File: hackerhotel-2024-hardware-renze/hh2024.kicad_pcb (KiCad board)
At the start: 2 copper layers, 95 parts, among them J1 SAO_connector, SW1 Multi-Directional-Switches, SW2 Multi-Directional-Switches, SW3 Multi-Directional-Switches, SW4 Multi-Directional-Switches, SW5 Multi-Directional-Switches

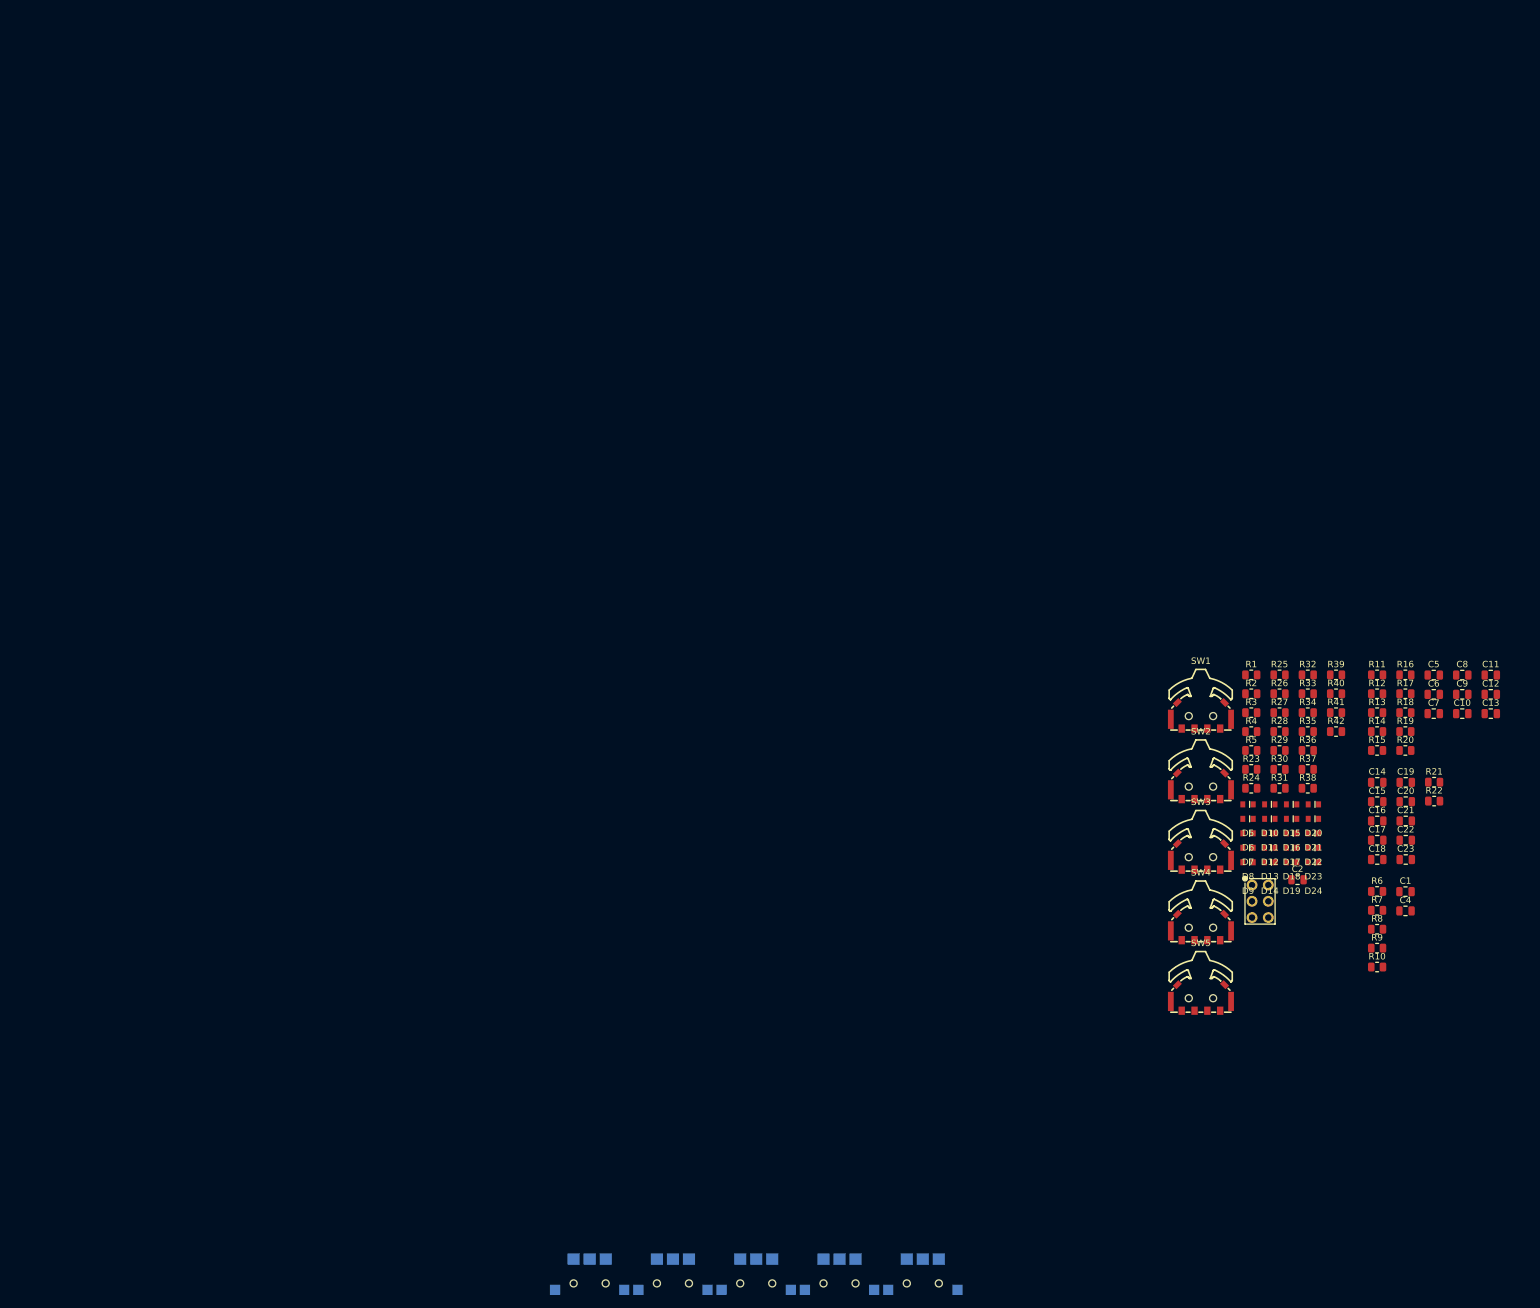
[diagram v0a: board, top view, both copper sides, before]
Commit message: Started layout
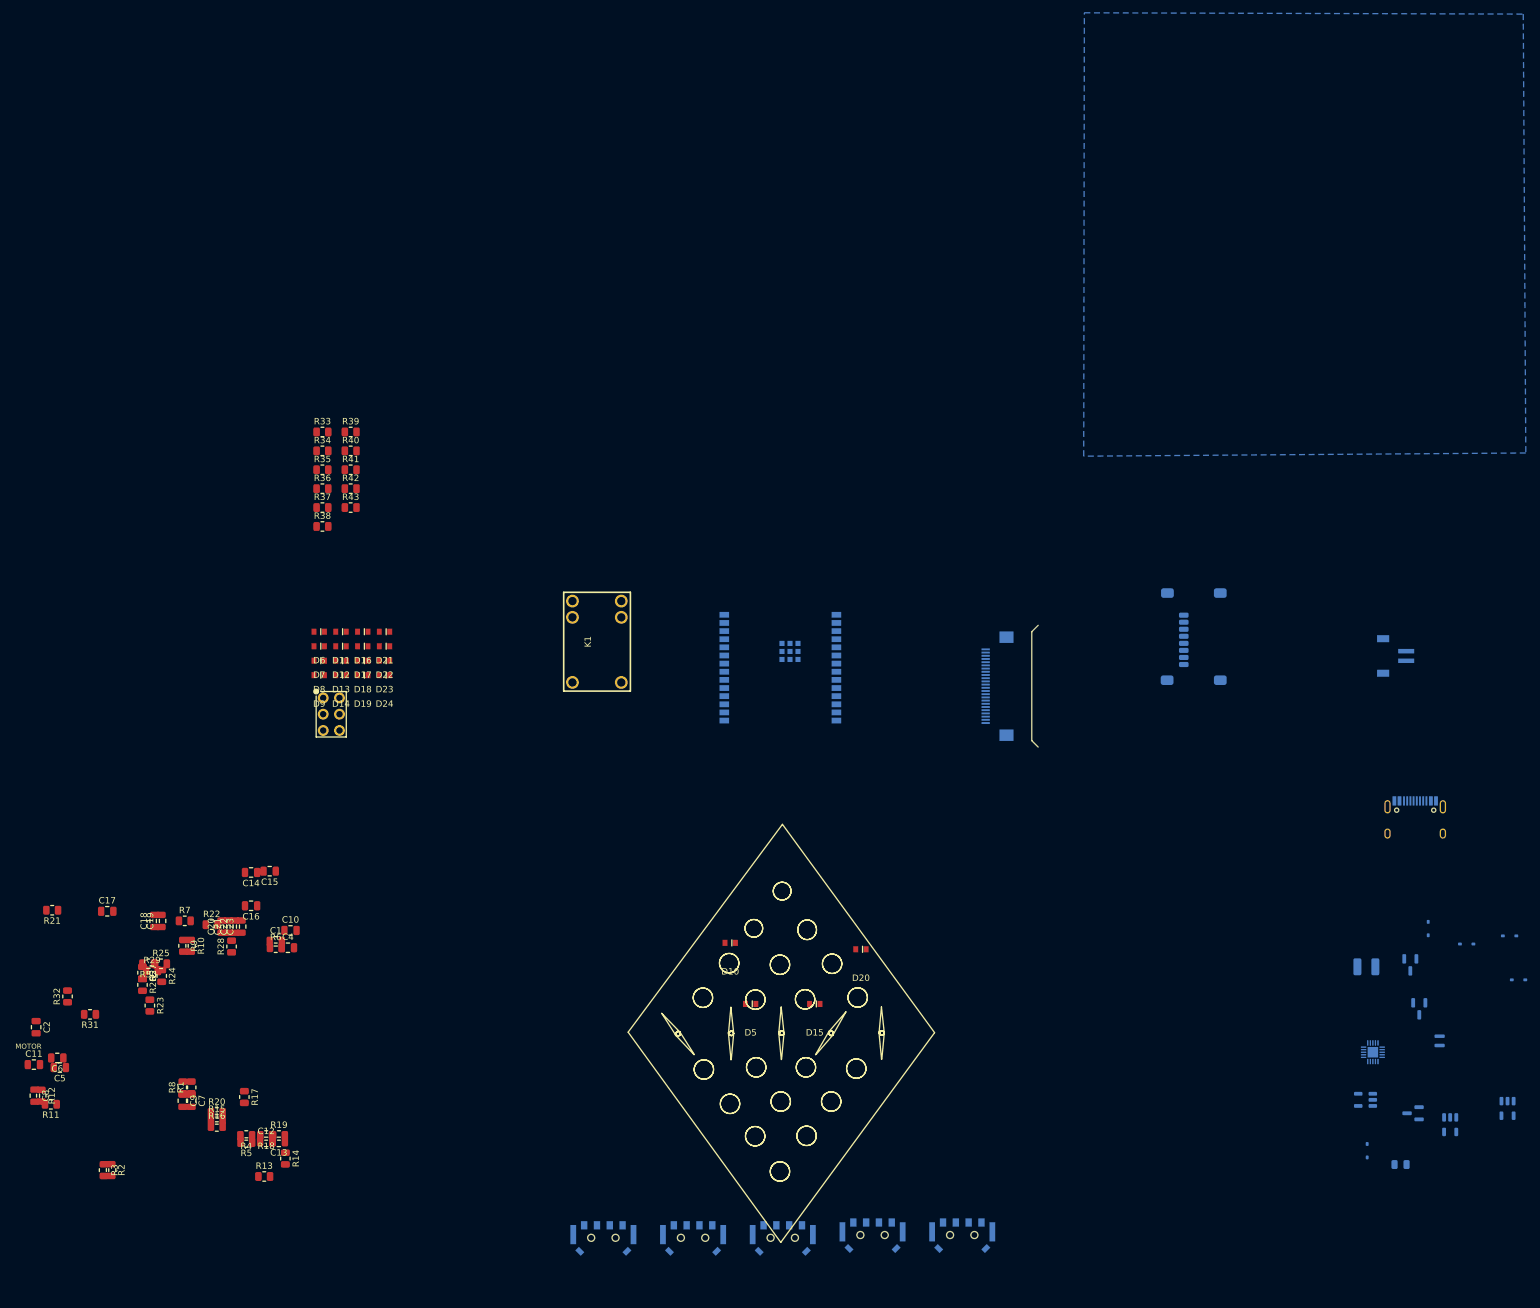
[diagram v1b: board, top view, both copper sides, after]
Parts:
- removed REF** (x5): TM-2022-2, BamboulabFootprints:TM-2022-2
- added D1: NSVR0320MW2T1G, tanoshii:D_SOD-323, B.Cu at (223.3, 138.5)
- added D2: NSVR0320MW2T1G, tanoshii:D_SOD-323, B.Cu at (245.6, 105.0)
- added D25: NSVR0320MW2T1G, tanoshii:D_SOD-323, B.Cu at (247.0, 111.8)
- added D3: NSVR0320MW2T1G, tanoshii:D_SOD-323, B.Cu at (238.9, 106.2)
- added D4: NSVR0320MW2T1G, tanoshii:D_SOD-323, B.Cu at (232.9, 103.8)
- added F1: 1A, tanoshii:Fuse_0805_2012Metric, B.Cu at (228.6, 140.7)
- added J3: Micro_SD_Card, tanoshii:MicroSD-SOFNG-TF-002-H18, B.Cu at (194.8, 58.2)
- added J4: USB-C, tanoshii:USB_C_Receptacle_HRO_TYPE-C-31-M-12, B.Cu at (230.8, 88.0)
- added J5: Battery, tanoshii:JST_S2B-ZR-SM4A-TF(LF)(SN), B.Cu at (227.3, 61.3)
- added J6: E-Paper, tanoshii:Hirose_FH12-24S-0.5SH_1x24-1MP_P0.50mm_Horizontal, B.Cu at (165.7, 66.0)
- added K1: SANYOU_SRD_Form_C, BamboulabFootprints:HRS1H-S-DC3V, F.Cu at (103.1, 59.1)
- added L1: 2.2u, tanoshii:Inductor_MSC20FC, B.Cu at (234.7, 121.4)
- added L2: 47u, tanoshii:L_1210_3225Metric, B.Cu at (223.2, 109.8)
- added Q1: AP2302B, tanoshii:SOT-23, B.Cu at (230.5, 132.7)
- added Q2: AP2302B, tanoshii:SOT-23, B.Cu at (230.1, 109.5)
- added Q3: AP2302B, tanoshii:SOT-23, B.Cu at (231.5, 116.4)
- added R43: 10k, Resistor_SMD:R_0805_2012Metric, F.Cu at (64.7, 38.1)
- added U1: ESP32-C6-WROOM-1, tanoshii:ESP32-C6-WROOM-1, B.Cu at (131.8, 63.1)
- added U2: SY8079AAC, tanoshii:SOT-23-5, B.Cu at (245.3, 131.9)
- added U3: XT4054K421MR-G, tanoshii:SOT-23-5, B.Cu at (236.3, 134.4)
- added U4: SY6280AAC, tanoshii:SOT-23-5, B.Cu at (223.1, 130.6)
- added U5: CH32V003F4U6, vfd:QFN-20-1EP_3x3mm_P0.4mm_EP1.65x1.65mm, B.Cu at (224.2, 123.1)
- J1: value SAO_connector -> SAO
- SW1, SW2, SW3, SW4, SW5: moved to B.Cu
- moved C11 235.4 mm to (15.3, 125.1)
- moved C8 232.3 mm to (15.4, 129.9), turned to -90 degrees
- moved C5 223.0 mm to (19.3, 125.5), turned to 180 degrees
- moved C6 222.2 mm to (18.9, 124.0), turned to 180 degrees
- moved R12 217.7 mm to (16.4, 129.9), turned to -90 degrees
- moved R11 217.6 mm to (17.9, 131.3), turned to 180 degrees
- moved R21 216.6 mm to (18.1, 101.0), turned to 180 degrees
- moved C9 209.5 mm to (38.5, 130.7), turned to -90 degrees
- moved C12 203.5 mm to (51.5, 137.1)
- moved C7 203.1 mm to (39.8, 130.7), turned to -90 degrees
- moved C13 200.6 mm to (53.5, 137.1), turned to 180 degrees
- moved R32 200.0 mm to (20.5, 114.4), turned to 90 degrees
- moved C17 198.5 mm to (26.7, 101.1)
- moved R16 198.4 mm to (43.8, 134.7)
- moved C2 198.2 mm to (15.6, 119.2), turned to -90 degrees
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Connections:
- J1 pad 5: unconnected-(J1-IO1-Pad5) -> /microcontroller/SAO IO1
- J1 pad 6: unconnected-(J1-IO2-Pad6) -> /microcontroller/SAO IO2
- R28 pad 2: MSW1L -> MSWL
- R29 pad 2: MSW1B -> MSWB
- R30 pad 2: MSW1R -> MSWR
- R31 pad 2: MSW2R -> MSWR
- R32 pad 2: MSW2B -> MSWB
- R33 pad 2: MSW2L -> MSWL
- R34 pad 2: MSW3R -> MSWR
- R35 pad 2: MSW3B -> MSWB
- R36 pad 2: MSW3L -> MSWL
- R37 pad 2: MSW4R -> MSWR
- R38 pad 2: MSW4B -> MSWB
- R39 pad 2: MSW4L -> MSWL
- R40 pad 2: MSW5R -> MSWR
- R41 pad 2: MSW5B -> MSWB
- R42 pad 2: MSW5L -> MSWL
- R8 pad 2: MSW2L -> /microcontroller/Relay Ctrl
- SW1 pad 1: GND -> MSWR
- SW1 pad 2: MSW1R -> MSWL
- SW1 pad C: (no net) -> MSWS1
- SW1 pad T: (no net) -> MSWB
- SW2 pad 1: GND -> MSWR
- SW2 pad 2: MSW2R -> MSWL
- SW2 pad C: (no net) -> MSWS2
- SW2 pad T: (no net) -> MSWB
- SW3 pad 1: GND -> MSWR
- SW3 pad 2: MSW3R -> MSWL
- SW3 pad C: (no net) -> MSWS3
- SW3 pad T: (no net) -> MSWB
- SW4 pad 1: unconnected-(SW4-C-Pad1) -> MSWR
- SW4 pad 2: MSW4R -> MSWL
- SW4 pad C: (no net) -> MSWS4
- SW4 pad T: (no net) -> MSWB
- SW5 pad 1: GND -> MSWR
- SW5 pad 2: MSW5R -> MSWL
- SW5 pad C: (no net) -> MSWS5
- SW5 pad T: (no net) -> MSWB
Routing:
- added copper zone on B.Cu, net GND
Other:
- board outline added: 1 x 19 mm
- board text added: "MOTOR"

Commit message: removed extra pull ups on multi switches
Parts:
- C1, C4, R10, R6, R7, R8, R9: moved to B.Cu
- R23, R24, R25, R26, R27: value R_Small -> 30
- moved R18 506.5 mm to (558.0, 139.7)
- moved R1 496.1 mm to (429.3, 436.0)
- moved C10 491.9 mm to (510.4, 290.8)
- moved C11 491.9 mm to (470.3, 311.8)
- moved C5 491.9 mm to (474.4, 312.2)
- moved C6 491.9 mm to (474.0, 310.7)
- moved C8 491.9 mm to (470.5, 316.6)
- moved R11 491.9 mm to (473.0, 318.0)
- moved R12 491.9 mm to (471.5, 316.6)
- moved C13 465.9 mm to (519.1, 152.4)
- moved R19 465.9 mm to (519.1, 151.4)
- moved J3 456.9 mm to (416.0, 458.0)
- moved R15 456.4 mm to (489.9, 230.1)
- moved R16 456.4 mm to (489.9, 231.2)
- moved R17 456.4 mm to (494.2, 226.6)
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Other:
- board size 1 x 19 mm -> 80 x 113 mm

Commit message: Routing complete (apart from LEDs)
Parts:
- removed R31, R32, R33, R34, R35, R36, R37, R38, R39, R40, R41, R42: 10k, Resistor_SMD:R_0805_2012Metric
- added J2: Breakout pads, Connector_PinHeader_2.54mm:PinHeader_1x03_P2.54mm_Vertical, B.Cu at (108.7, 64.8)
- C10, C11, C12, C13, C14, C15, C16, C17, C18, C19, C2, C20, C21, C22, C23, C5, C6, C7, C8, C9, D10, D11, D12, D13, D14, D15, D16, D17, D18, D19, D20, D21, D22, D23, D24, D5, D6, D7, D8, D9, J1, R1, R11, R12, R13, R14, R15, R16, R17, R18, R19, R2, R20, R21, R22, R23, R24, R25, R26, R27, R28, R29, R3, R30, R4, R43, R5: moved to B.Cu
- moved J3 513.4 mm to (96.8, 55.8)
- moved R1 498.8 mm to (107.7, 54.6)
- moved R18 457.4 mm to (102.7, 95.5), turned to 0 degrees
- moved C13 426.4 mm to (97.1, 91.4)
- moved R19 426.0 mm to (97.1, 93.5)
- moved U2 425.2 mm to (149.8, 90.3)
- moved D1 418.9 mm to (121.4, 84.2), turned to 90 degrees
- moved Q1 414.4 mm to (130.8, 85.2), turned to 0 degrees
- moved C10 414.4 mm to (149.8, 86.7), turned to 180 degrees
- moved U4 412.9 mm to (124.2, 85.3), turned to -90 degrees
- moved L1 409.3 mm to (152.7, 88.1), turned to -90 degrees
- moved R12 400.5 mm to (143.3, 87.2), turned to 180 degrees
- moved C8 398.4 mm to (143.3, 89.3), turned to 180 degrees
- moved R11 397.8 mm to (145.2, 92.6), turned to -90 degrees
- moved R15 395.1 mm to (124.4, 80.0)
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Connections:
- K1 pad 1: unconnected-(K1-Pad1) -> Net-(J2-Pin_3)
- K1 pad 3: unconnected-(K1-Pad3) -> Net-(J2-Pin_2)
- K1 pad 4: unconnected-(K1-Pad4) -> Net-(J2-Pin_1)
- U5 pad 10: MSWS2 -> LED D
- U5 pad 16: LED A -> MSWS5
- U5 pad 17: LED B -> MSWS4
- U5 pad 18: LED C -> MSWS3
- U5 pad 19: LED D -> MSWS2
- U5 pad 2: MSWS1 -> LED C
- U5 pad 20: LED E -> MSWS1
- U5 pad 3: MSWS4 -> LED E
- U5 pad 5: MSWS5 -> LED A
- U5 pad 7: MSWS3 -> LED B
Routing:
- net +3V3: track 0.00 -> 226.1 mm
- net MSWL: track 0.00 -> 84.1 mm
- net /E-Paper/SCK: track 0.00 -> 80.9 mm, vias 0 -> 4
- net MSWS1: track 0.00 -> 80.5 mm
- net /E-Paper/MOSI: track 0.00 -> 79.8 mm, vias 0 -> 2
- net SDA: track 0.00 -> 72.5 mm, vias 0 -> 2
- net VIN: track 0.00 -> 71.2 mm, vias 0 -> 2
- net SCL: track 0.00 -> 71.2 mm, vias 0 -> 2
- net MSWS2: track 0.00 -> 67.0 mm
- net MSWB: track 0.00 -> 66.5 mm
- net GND: track 0.00 -> 64.4 mm, vias 0 -> 6
- net /E-Paper/RESET: track 0.00 -> 57.9 mm, vias 0 -> 2
- net /Power management/SENSE: track 0.00 -> 55.3 mm, vias 0 -> 2
- net MSWS3: track 0.00 -> 53.5 mm
- net /microcontroller/D-: track 0.00 -> 51.5 mm, vias 0 -> 4
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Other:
- board text added: "3.3V Regulator"
- board text added: "Battery/Charger"
- board text added: "Display"
- board text added: "Power Switch"

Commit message: routing almost finished
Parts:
- added R31: 100k, Resistor_SMD:R_0805_2012Metric, B.Cu at (98.3, 76.5)
- added SW6: SW_SPDT, Button_Switch_SMD:SW_SPDT_PCM12, B.Cu at (94.0, 78.0)
- moved D13 95.2 mm to (139.8, 107.8), turned to 0 degrees
- moved D8 92.7 mm to (135.9, 102.1), turned to 0 degrees
- moved D7 92.3 mm to (132.1, 96.0), turned to 0 degrees
- moved D5 90.8 mm to (127.8, 113.3), turned to 0 degrees
- moved D6 90.6 mm to (143.8, 113.3), turned to 0 degrees
- moved D14 89.9 mm to (131.7, 107.9), turned to 0 degrees
- moved D10 87.8 mm to (135.7, 113.4), turned to 0 degrees
- moved D12 87.5 mm to (127.6, 102.1), turned to 0 degrees
- moved D11 79.7 mm to (123.8, 107.6), turned to 0 degrees
- moved D9 74.6 mm to (119.7, 113.3), turned to 0 degrees
- moved F1 16.8 mm to (101.0, 97.2)
- moved J4 16.8 mm to (94.6, 91.1)
- moved R4 16.8 mm to (101.0, 93.7)
- moved R5 16.8 mm to (101.0, 88.6)
- moved C13 10.9 mm to (107.9, 92.9)
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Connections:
- D10 pad 2: /B -> /D
- D11 pad 1: /A -> /C
- D11 pad 2: /B -> /D
- D12 pad 2: /A -> /C
- D13 pad 2: /A -> /C
- D15 pad 1: /A -> /E
- D15 pad 2: /B -> /D
- D16 pad 1: /B -> /D
- D16 pad 2: /A -> /C
- D17 pad 1: /A -> /E
- D17 pad 2: /A -> /C
- D18 pad 1: /A -> /C
- D19 pad 1: /B -> /D
- D20 pad 1: /A -> /E
- D22 pad 1: /A -> /C
- D23 pad 1: /B -> /D
- D24 pad 1: /A -> /E
- D5 pad 2: /A -> /E
- D6 pad 2: /A -> /E
- D7 pad 1: /A -> /C
- D7 pad 2: /A -> /E
- D8 pad 1: /B -> /D
- D8 pad 2: /A -> /E
- D9 pad 2: /B -> /D
- R17 pad 1: VBAT -> Net-(SW6-B)
- R23 pad 2: /A -> /E
- R24 pad 2: /B -> /D
- R25 pad 2: /A -> /C
- U4 pad 5: VBAT -> Net-(SW6-B)
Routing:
- net MSWR: track 2.83 -> 101.8 mm, vias 0 -> 7
- net Net-(SW6-B): track 0.00 -> 63.3 mm
- net /E: track 0.00 -> 58.4 mm
- net /D: track 0.00 -> 41.0 mm
- net /microcontroller/CH32 Prog: track 50.3 -> 90.9 mm, vias 2 -> 4
- net MSWB: track 66.5 -> 101.5 mm
- net MSWL: track 84.1 -> 114.6 mm, vias 0 -> 2
- net /microcontroller/Low Pow CH32: track 41.6 -> 69.6 mm, vias 2 -> 4
- net /A: track 0.00 -> 27.7 mm
- net /C: track 0.00 -> 21.6 mm
- net /B: track 0.00 -> 15.3 mm
- net /microcontroller/D-: track 51.5 -> 65.7 mm
- net /microcontroller/D+: track 48.8 -> 62.9 mm
- net VUSB: track 49.2 -> 41.9 mm, vias 0 -> 2
- net VBAT: track 31.9 -> 38.5 mm
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- added copper zone on F.Cu, net GND
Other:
- board text removed: "MOTOR"
